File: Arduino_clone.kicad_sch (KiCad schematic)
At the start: 0 parts

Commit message: added
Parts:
- added BT?: Battery, symbol Device:Battery
- added C? (x2): C, symbol Device:C
- added C?: C_Polarized, symbol Device:C_Polarized
- added D?: LED, symbol Device:LED
- added R? (x2): R, symbol Device:R
- added U?: 24LC1025, symbol Memory_EEPROM:24LC1025
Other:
- added sheet connectors (connectors.kicad_sch)
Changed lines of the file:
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@@
     (comment 1 "Designed by Bernard")
+  )
+  (symbol (lib_id "Device:C") (at 137.16 74.93 0) (unit 1)
+    (in_bom yes) (on_board yes) (fields_autoplaced)
+    (property "Reference" "C?" (id 0) (at 140.97 73.6599 0)
+      (effects (font (size 1.27 1.27)) (justify left))
+    )
+    (property "Value" "C" (id 1) (at 140.97 76.1999 0)
+      (effects (font (size 1.27 1.27)) (justify left))
+    )
+    (property "Footprint" "" (id 2) (at 138.1252 78.74 0)
+      (effects (font (size 1.27 1.27)) hide)
+    )
+    (property "Datasheet" "~" (id 3) (at 137.16 74.93 0)
+      (effects (font (size 1.27 1.27)) hide)
+    )
+    (pin "1")
+    (pin "2")
+  )
+  (symbol (lib_id "Device:Battery") (at 97.79 64.77 0) (unit 1)
+    (in_bom yes) (on_board yes) (fields_autoplaced)
+    (property "Reference" "BT?" (id 0) (at 101.6 63.1189 0)
+      (effects (font (size 1.27 1.27)) (justify left))
+    )
+    (property "Value" "Battery" (id 1) (at 101.6 65.6589 0)
+      (effects (font (size 1.27 1.27)) (justify left))
+    )
+    (property "Footprint" "" (id 2) (at 97.79 63.246 90)
+      (effects (font (size 1.27 1.27)) hide)
+    )
+    (property "Datasheet" "~" (id 3) (at 97.79 63.246 90)
+      (effects (font (size 1.27 1.27)) hide)
+    )
+    (pin "1")
+    (pin "2")
+  )
+  (symbol (lib_id "Device:C") (at 137.16 60.96 0) (unit 1)
+    (in_bom yes) (on_board yes) (fields_autoplaced)
+    (property "Reference" "C?" (id 0) (at 140.97 59.6899 0)
+      (effects (font (size 1.27 1.27)) (justify left))
+    )
+    (property "Value" "C" (id 1) (at 140.97 62.2299 0)
+      (effects (font (size 1.27 1.27)) (justify left))
+    )
+    (property "Footprint" "" (id 2) (at 138.1252 64.77 0)
+      (effects (font (size 1.27 1.27)) hide)
+    )
+    (property "Datasheet" "~" (id 3) (at 137.16 60.96 0)
+      (effects (font (size 1.27 1.27)) hide)
+    )
+    (pin "1")
+    (pin "2")
+  )
+  (symbol (lib_id "Device:LED") (at 99.06 87.63 0) (unit 1)
+    (in_bom yes) (on_board yes) (fields_autoplaced)
+    (property "Reference" "D?" (id 0) (at 97.4725 81.28 0))
+    (property "Value" "LED" (id 1) (at 97.4725 83.82 0))
+    (property "Footprint" "" (id 2) (at 99.06 87.63 0)
+      (effects (font (size 1.27 1.27)) hide)
+    )
+    (property "Datasheet" "~" (id 3) (at 99.06 87.63 0)
+      (effects (font (size 1.27 1.27)) hide)
+    )
+    (pin "1")
+    (pin "2")
+  )
+  (symbol (lib_id "Device:R") (at 162.56 74.93 0) (unit 1)
+    (in_bom yes) (on_board yes) (fields_autoplaced)
+    (property "Reference" "R?" (id 0) (at 165.1 73.6599 0)
+      (effects (font (size 1.27 1.27)) (justify left))
+    )
+    (property "Value" "R" (id 1) (at 165.1 76.1999 0)
+      (effects (font (size 1.27 1.27)) (justify left))
+    )
+    (property "Footprint" "" (id 2) (at 160.782 74.93 90)
+      (effects (font (size 1.27 1.27)) hide)
+    )
+    (property "Datasheet" "~" (id 3) (at 162.56 74.93 0)
+      (effects (font (size 1.27 1.27)) hide)
+    )
+    (pin "1")
+    (pin "2")
+  )
+  (symbol (lib_id "Device:R") (at 162.56 58.42 0) (unit 1)
+    (in_bom yes) (on_board yes) (fields_autoplaced)
+    (property "Reference" "R?" (id 0) (at 165.1 57.1499 0)
+      (effects (font (size 1.27 1.27)) (justify left))
+    )
+    (property "Value" "R" (id 1) (at 165.1 59.6899 0)
+      (effects (font (size 1.27 1.27)) (justify left))
+    )
+    (property "Footprint" "" (id 2) (at 160.782 58.42 90)
+      (effects (font (size 1.27 1.27)) hide)
+    )
+    (property "Datasheet" "~" (id 3) (at 162.56 58.42 0)
+      (effects (font (size 1.27 1.27)) hide)
+    )
+    (pin "1")
+    (pin "2")
+  )
+  (symbol (lib_id "Device:C_Polarized") (at 137.16 92.71 0) (unit 1)
+    (in_bom yes) (on_board yes) (fields_autoplaced)
+    (property "Reference" "C?" (id 0) (at 140.97 90.5509 0)
+      (effects (font (size 1.27 1.27)) (justify left))
+    )
+    (property "Value" "C_Polarized" (id 1) (at 140.97 93.0909 0)
+      (effects (font (size 1.27 1.27)) (justify left))
+    )
+    (property "Footprint" "" (id 2) (at 138.1252 96.52 0)
+      (effects (font (size 1.27 1.27)) hide)
+    )
+    (property "Datasheet" "~" (id 3) (at 137.16 92.71 0)
+      (effects (font (size 1.27 1.27)) hide)
+    )
+    (pin "1")
+    (pin "2")
+  )
+  (symbol (lib_id "Memory_EEPROM:24LC1025") (at 195.58 52.07 0) (unit 1)
+    (in_bom yes) (on_board yes) (fields_autoplaced)
+    (property "Reference" "U?" (id 0) (at 197.5994 41.91 0)
+      (effects (font (size 1.27 1.27)) (justify left))
+    )
+    (property "Value" "24LC1025" (id 1) (at 197.5994 44.45 0)
+      (effects (font (size 1.27 1.27)) (justify left))
+    )
+    (property "Footprint" "" (id 2) (at 195.58 52.07 0)
+      (effects (font (size 1.27 1.27)) hide)
+    )
+    (property "Datasheet" "http://ww1.microchip.com/downloads/en/DeviceDoc/21941B.pdf" (id 3) (at 195.58 52.07 0)
+      (effects (font (size 1.27 1.27)) hide)
+    )
+    (pin "1")
+    (pin "2")
+    (pin "3")
+    (pin "4")
+    (pin "5")
+    (pin "6")
+    (pin "7")
+    (pin "8")
+  )
+  (sheet (at 186.69 77.47) (size 53.34 74.93) (fields_autoplaced)
+    (stroke (width 0.1524) (type solid) (color 0 0 0 0))
+    (fill (color 0 0 0 0.0000))
+    (property "Sheet name" "connectors" (id 0) (at 186.69 76.7584 0)
+      (effects (font (size 1.27 1.27)) (justify left bottom))
+    )
+    (property "Sheet file" "connectors.kicad_sch" (id 1) (at 186.69 152.9846 0)
+      (effects (font (size 1.27 1.27)) (justify left top))
+    )
   )
   (sheet_instances
     (path "/" (page "1"))
+    (path "/624c948a-ecca-425f-9ead-8d91c4f678af" (page "2"))
+  )
+  (symbol_instances
+    (path "/19cd3de1-faa9-409c-93a7-570d16f1bc1e"
+      (reference "BT?") (unit 1) (value "Battery") (footprint "")
+    )
+    (path "/08cdfe5b-2ba9-4b3b-bc2e-50dad6062b2c"
+      (reference "C?") (unit 1) (value "C") (footprint "")
+    )
+    (path "/47813852-57ce-4b02-8beb-d3c09229f1ca"
+      (reference "C?") (unit 1) (value "C") (footprint "")
+    )
+    (path "/e708e5c5-7d07-45f8-89e3-31ce5f8c8f07"
+      (reference "C?") (unit 1) (value "C_Polarized") (footprint "")
+    )
+    (path "/b54f1df4-ba03-4859-9ba4-5773c266358f"
+      (reference "D?") (unit 1) (value "LED") (footprint "")
+    )
+    (path "/624c948a-ecca-425f-9ead-8d91c4f678af/1765874c-728c-40bc-a850-d1f5b68a4351"
+      (reference "J?") (unit 1) (value "Conn_01x09_Male") (footprint "")
+    )
+    (path "/624c948a-ecca-425f-9ead-8d91c4f678af/44d4a4b7-200c-41e2-b17e-ae05624e8fef"
+      (reference "J?") (unit 1) (value "Conn_01x04_Male") (footprint "")
+    )
+    (path "/624c948a-ecca-425f-9ead-8d91c4f678af/60e50561-d38f-4138-a215-443f5e3ca19f"
+      (reference "J?") (unit 1) (value "Conn_02x03_Odd_Even") (footprint "")
+    )
+    (path "/624c948a-ecca-425f-9ead-8d91c4f678af/b3b923ac-a53a-4e93-a25a-a598d0730a0f"
+      (reference "J?") (unit 1) (value "Conn_01x04_Male") (footprint "")
+    )
+    (path "/c652f6e4-562a-4981-8ce5-c0d8eae9a6ef"
+      (reference "R?") (unit 1) (value "R") (footprint "")
+    )
+    (path "/d5929be8-1b2e-4cd0-b3aa-731b0029a5d8"
+      (reference "R?") (unit 1) (value "R") (footprint "")
+    )
+    (path "/f1a52e3f-9a31-46d1-962a-ccc45437db9a"
+      (reference "U?") (unit 1) (value "24LC1025") (footprint "")
+    )
   )
 )

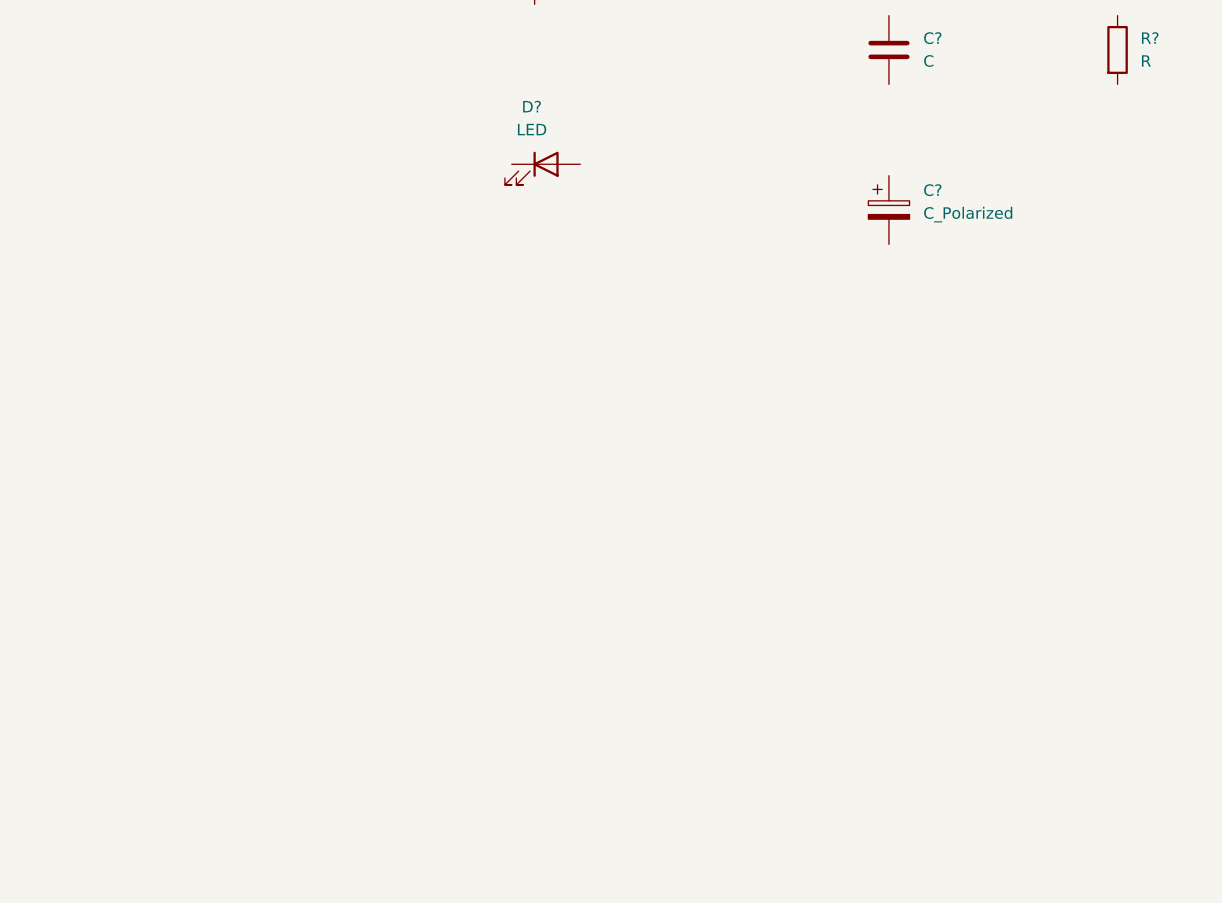
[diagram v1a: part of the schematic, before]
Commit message: creating a new symbol for the clock
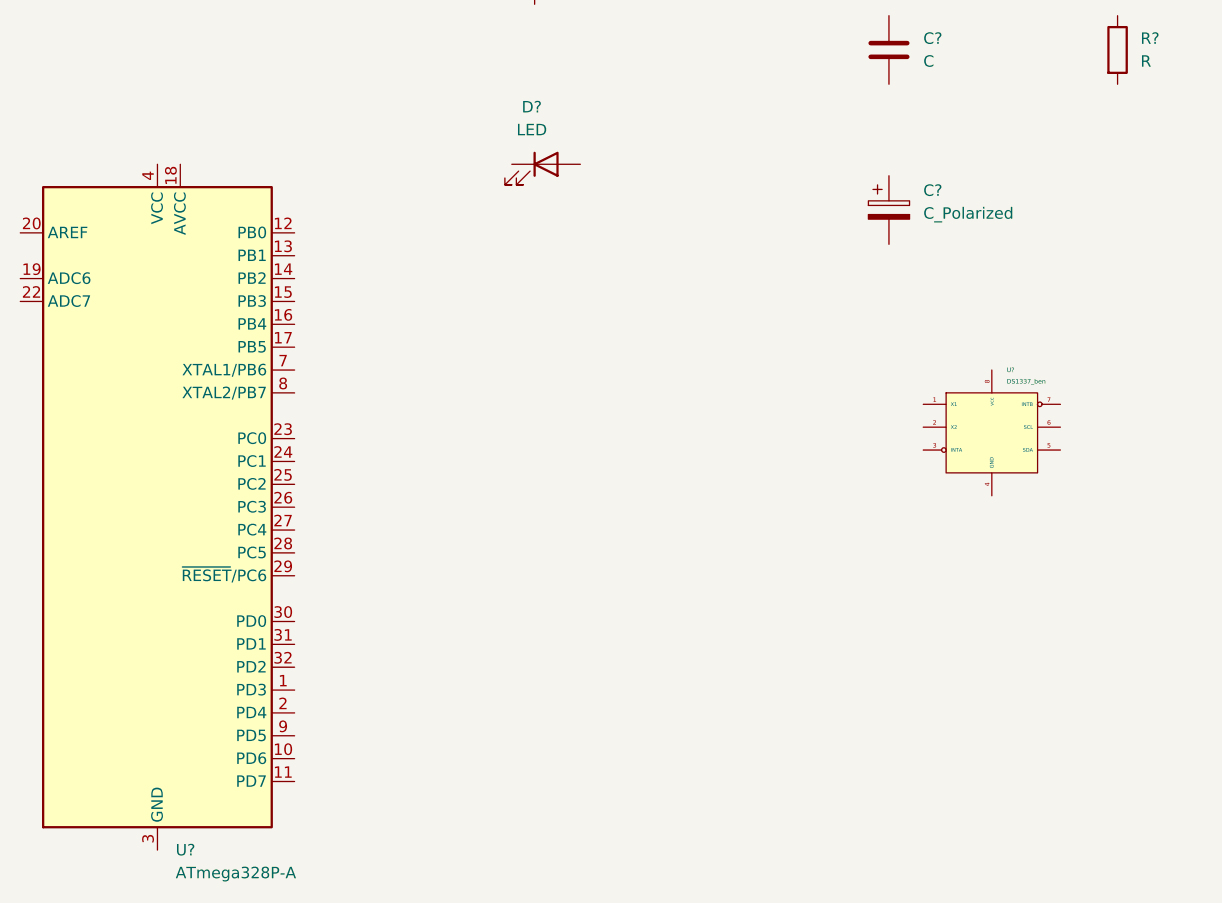
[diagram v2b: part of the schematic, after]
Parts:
- added U?: ATmega328P-A, Package_QFP:TQFP-32_7x7mm_P0.8mm, symbol MCU_Microchip_ATmega:ATmega328P-A
- added U?: DS1337_ben, symbol New_Library:DS1337_ben
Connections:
- new net: U?.21 (GND), U?.3 (GND), U?.5 (GND)
- new net: U?.4 (VCC), U?.6 (VCC)
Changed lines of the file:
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@@
     (pin "2")
+  )
+  (symbol (lib_id "MCU_Microchip_ATmega:ATmega328P-A") (at 55.88 125.73 0) (unit 1)
+    (in_bom yes) (on_board yes) (fields_autoplaced)
+    (property "Reference" "U?" (id 0) (at 57.8994 163.83 0)
+      (effects (font (size 1.27 1.27)) (justify left))
+    )
+    (property "Value" "ATmega328P-A" (id 1) (at 57.8994 166.37 0)
+      (effects (font (size 1.27 1.27)) (justify left))
+    )
+    (property "Footprint" "Package_QFP:TQFP-32_7x7mm_P0.8mm" (id 2) (at 55.88 125.73 0)
+      (effects (font (size 1.27 1.27) italic) hide)
+    )
+    (property "Datasheet" "http://ww1.microchip.com/downloads/en/DeviceDoc/ATmega328_P%20AVR%20MCU%20with%20picoPower%20Technology%20Data%20Sheet%2040001984A.pdf" (id 3) (at 55.88 125.73 0)
+      (effects (font (size 1.27 1.27)) hide)
+    )
+    (pin "1")
+    (pin "10")
+    (pin "11")
+    (pin "12")
+    (pin "13")
+    (pin "14")
+    (pin "15")
+    (pin "16")
+    (pin "17")
+    (pin "18")
+    (pin "19")
+    (pin "2")
+    (pin "20")
+    (pin "21")
+    (pin "22")
+    (pin "23")
+    (pin "24")
+    (pin "25")
+    (pin "26")
+    (pin "27")
+    (pin "28")
+    (pin "29")
+    (pin "3")
+    (pin "30")
+    (pin "31")
+    (pin "32")
+    (pin "4")
+    (pin "5")
+    (pin "6")
+    (pin "7")
+    (pin "8")
+    (pin "9")
   )
   (symbol (lib_id "Device:LED") (at 99.06 87.63 0) (unit 1)
@@
     (pin "2")
   )
-  (symbol (lib_id "Device:R") (at 162.56 58.42 0) (unit 1)
-    (in_bom yes) (on_board yes) (fields_autoplaced)
-    (property "Reference" "R?" (id 0) (at 165.1 57.1499 0)
-      (effects (font (size 1.27 1.27)) (justify left))
-    )
-    (property "Value" "R" (id 1) (at 165.1 59.6899 0)
-      (effects (font (size 1.27 1.27)) (justify left))
-    )
-    (property "Footprint" "" (id 2) (at 160.782 58.42 90)
-      (effects (font (size 1.27 1.27)) hide)
-    )
-    (property "Datasheet" "~" (id 3) (at 162.56 58.42 0)
-      (effects (font (size 1.27 1.27)) hide)
-    )
-    (pin "1")
-    (pin "2")
-  )
-  (symbol (lib_id "Device:C_Polarized") (at 137.16 92.71 0) (unit 1)
-    (in_bom yes) (on_board yes) (fields_autoplaced)
-    (property "Reference" "C?" (id 0) (at 140.97 90.5509 0)
-      (effects (font (size 1.27 1.27)) (justify left))
-    )
-    (property "Value" "C_Polarized" (id 1) (at 140.97 93.0909 0)
-      (effects (font (size 1.27 1.27)) (justify left))
-    )
-    (property "Footprint" "" (id 2) (at 138.1252 96.52 0)
-      (effects (font (size 1.27 1.27)) hide)
-    )
-    (property "Datasheet" "~" (id 3) (at 137.16 92.71 0)
-      (effects (font (size 1.27 1.27)) hide)
-    )
-    (pin "1")
-    (pin "2")
-  )
-  (symbol (lib_id "Memory_EEPROM:24LC1025") (at 195.58 52.07 0) (unit 1)
-    (in_bom yes) (on_board yes) (fields_autoplaced)
-    (property "Reference" "U?" (id 0) (at 197.5994 41.91 0)
-      (effects (font (size 1.27 1.27)) (justify left))
-    )
-    (property "Value" "24LC1025" (id 1) (at 197.5994 44.45 0)
-      (effects (font (size 1.27 1.27)) (justify left))
-    )
-    (property "Footprint" "" (id 2) (at 195.58 52.07 0)
-      (effects (font (size 1.27 1.27)) hide)
-    )
-    (property "Datasheet" "http://ww1.microchip.com/downloads/en/DeviceDoc/21941B.pdf" (id 3) (at 195.58 52.07 0)
+  (symbol (lib_id "New_Library:DS1337_ben") (at 148.59 118.11 0) (unit 1)
+    (in_bom yes) (on_board yes) (fields_autoplaced)
+    (property "Reference" "U?" (id 0) (at 150.2411 110.49 0)
+      (effects (font (size 0.5 0.5)) (justify left))
+    )
+    (property "Value" "DS1337_ben" (id 1) (at 150.2411 111.76 0)
+      (effects (font (size 0.5 0.5)) (justify left))
+    )
+    (property "Footprint" "" (id 2) (at 148.59 113.03 0)
+      (effects (font (size 1.27 1.27)) hide)
+    )
+    (property "Datasheet" "" (id 3) (at 148.59 113.03 0)
       (effects (font (size 1.27 1.27)) hide)
     )
@@
     (pin "8")
   )
+  (symbol (lib_id "Device:R") (at 162.56 58.42 0) (unit 1)
+    (in_bom yes) (on_board yes) (fields_autoplaced)
+    (property "Reference" "R?" (id 0) (at 165.1 57.1499 0)
+      (effects (font (size 1.27 1.27)) (justify left))
+    )
+    (property "Value" "R" (id 1) (at 165.1 59.6899 0)
+      (effects (font (size 1.27 1.27)) (justify left))
+    )
+    (property "Footprint" "" (id 2) (at 160.782 58.42 90)
+      (effects (font (size 1.27 1.27)) hide)
+    )
+    (property "Datasheet" "~" (id 3) (at 162.56 58.42 0)
+      (effects (font (size 1.27 1.27)) hide)
+    )
+    (pin "1")
+    (pin "2")
+  )
+  (symbol (lib_id "Device:C_Polarized") (at 137.16 92.71 0) (unit 1)
+    (in_bom yes) (on_board yes) (fields_autoplaced)
+    (property "Reference" "C?" (id 0) (at 140.97 90.5509 0)
+      (effects (font (size 1.27 1.27)) (justify left))
+    )
+    (property "Value" "C_Polarized" (id 1) (at 140.97 93.0909 0)
+      (effects (font (size 1.27 1.27)) (justify left))
+    )
+    (property "Footprint" "" (id 2) (at 138.1252 96.52 0)
+      (effects (font (size 1.27 1.27)) hide)
+    )
+    (property "Datasheet" "~" (id 3) (at 137.16 92.71 0)
+      (effects (font (size 1.27 1.27)) hide)
+    )
+    (pin "1")
+    (pin "2")
+  )
+  (symbol (lib_id "Memory_EEPROM:24LC1025") (at 195.58 52.07 0) (unit 1)
+    (in_bom yes) (on_board yes) (fields_autoplaced)
+    (property "Reference" "U?" (id 0) (at 197.5994 41.91 0)
+      (effects (font (size 1.27 1.27)) (justify left))
+    )
+    (property "Value" "24LC1025" (id 1) (at 197.5994 44.45 0)
+      (effects (font (size 1.27 1.27)) (justify left))
+    )
+    (property "Footprint" "" (id 2) (at 195.58 52.07 0)
+      (effects (font (size 1.27 1.27)) hide)
+    )
+    (property "Datasheet" "http://ww1.microchip.com/downloads/en/DeviceDoc/21941B.pdf" (id 3) (at 195.58 52.07 0)
+      (effects (font (size 1.27 1.27)) hide)
+    )
+    (pin "1")
+    (pin "2")
+    (pin "3")
+    (pin "4")
+    (pin "5")
+    (pin "6")
+    (pin "7")
+    (pin "8")
+  )
   (sheet (at 186.69 77.47) (size 53.34 74.93) (fields_autoplaced)
     (stroke (width 0.1524) (type solid) (color 0 0 0 0))
@@
       (reference "R?") (unit 1) (value "R") (footprint "")
     )
+    (path "/8f2d2642-dcfa-4ad9-ac92-8f59bebb14c5"
+      (reference "U?") (unit 1) (value "ATmega328P-A") (footprint "Package_QFP:TQFP-32_7x7mm_P0.8mm")
+    )
+    (path "/d2bd4747-c7d7-47fd-8472-b788c1702d24"
+      (reference "U?") (unit 1) (value "DS1337_ben") (footprint "")
+    )
     (path "/f1a52e3f-9a31-46d1-962a-ccc45437db9a"
